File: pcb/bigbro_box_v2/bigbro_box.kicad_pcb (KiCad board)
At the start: 2 copper layers, 100 x 58 mm, 46 parts, among them J1 Current Sense, J2 Display, J3 Mains, J4 Debug, J5 RFID, J6 Relay, J7 Ext, K1 G5LE-1, Q1 MMBT3904, Q2 MMBT3904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

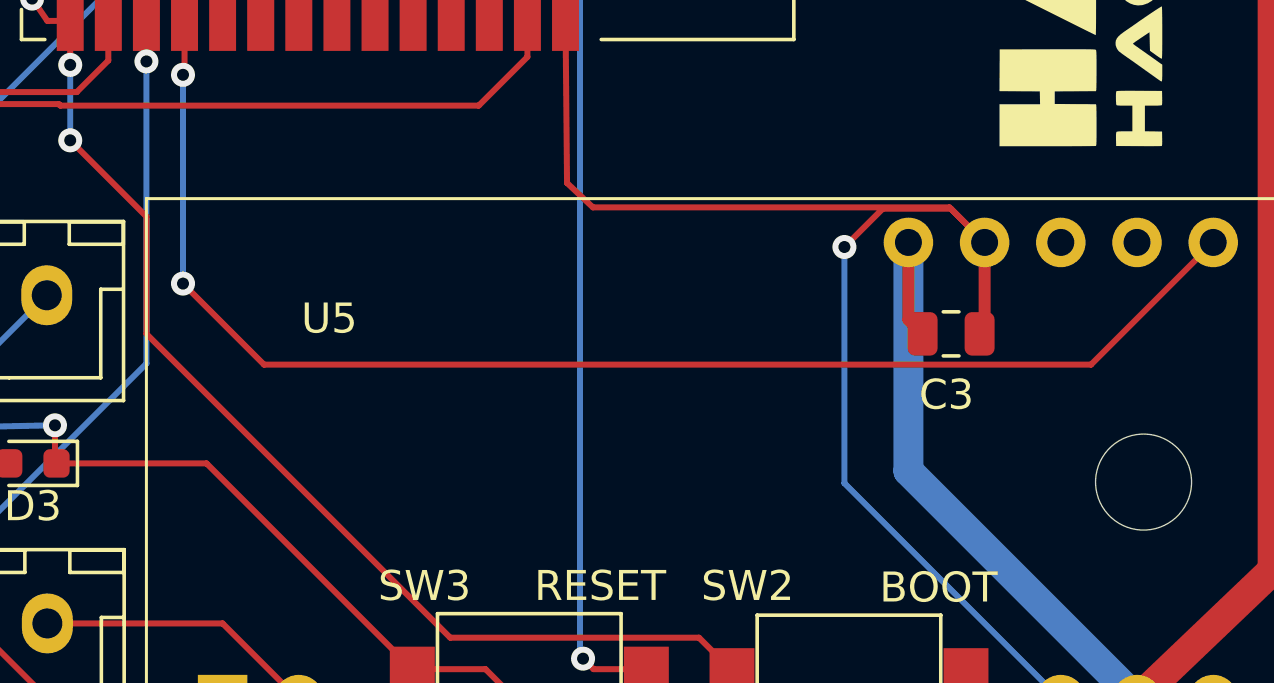
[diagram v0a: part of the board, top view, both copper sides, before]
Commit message: Add voltage divider for RFID.
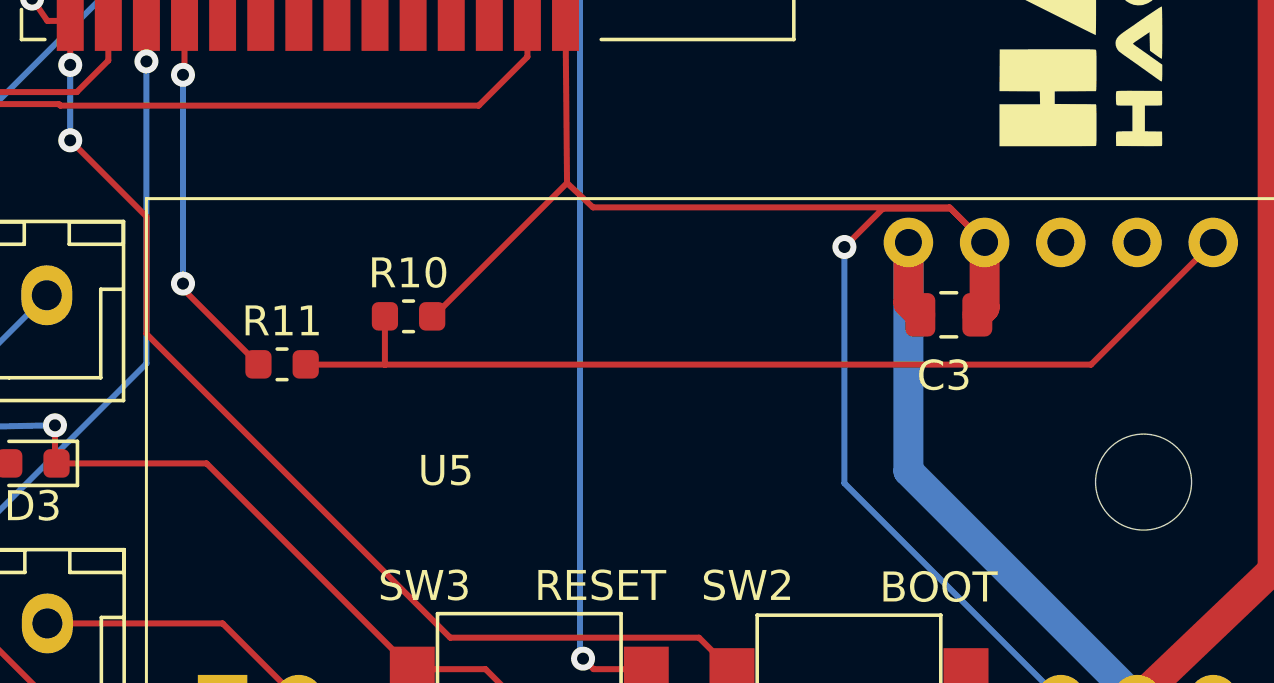
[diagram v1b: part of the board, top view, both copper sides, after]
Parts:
- added R10: 2k2, Resistor_SMD:R_0603_1608Metric, F.Cu at (136.5, 98.5)
- added R11: 1k2, Resistor_SMD:R_0603_1608Metric, F.Cu at (132.3, 100.1)
- moved C3 0.64 mm to (154.5, 98.4)
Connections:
- U5 pad 6: ESP_RFID_TX -> Net-(U5-TX)
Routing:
- net Net-(U5-TX): track 0.00 -> 33.6 mm
- net ESP_RFID_TX: track 45.9 -> 12.5 mm
- net GND: track 317.4 -> 323.1 mm
- net +5V: track 197.9 -> 197.3 mm

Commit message: Increase value of switch LED resistor.
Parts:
- R9: value 330 -> 680
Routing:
- net /~{BOOT}: track 67.5 -> 69.3 mm
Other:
- board text added: "https://github.com/hal9k-dk/bigbro"

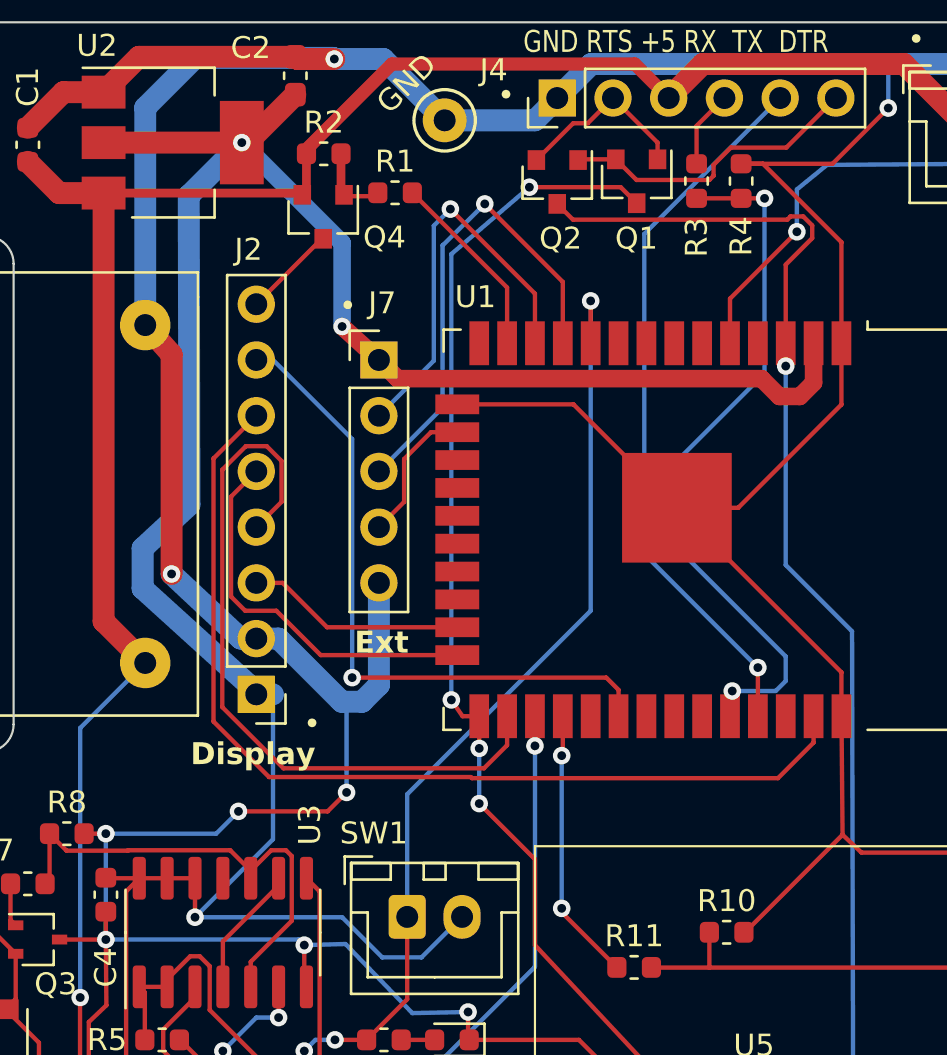
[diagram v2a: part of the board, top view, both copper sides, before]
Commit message: Flip display connector.
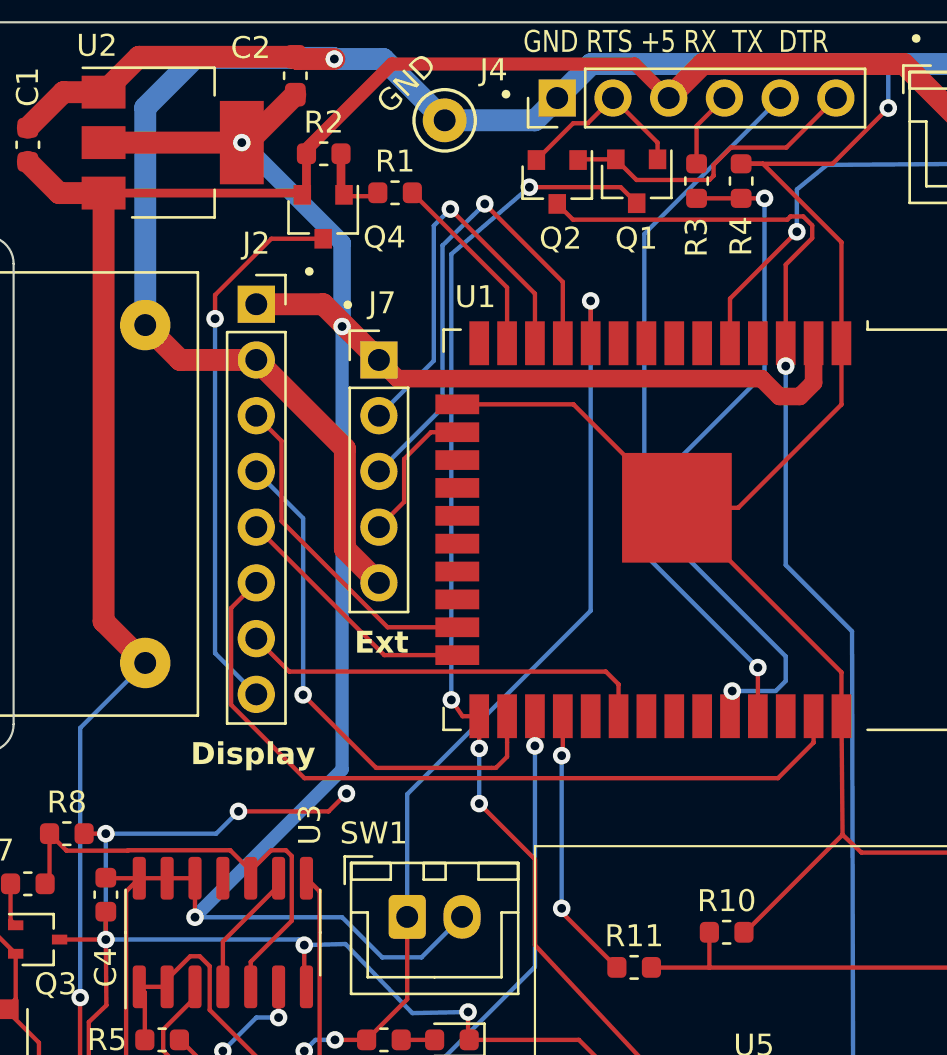
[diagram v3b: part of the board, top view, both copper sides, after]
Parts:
- J2: footprint Connector_PinHeader_2.54mm:PinHeader_1x08_P2.54mm_Vertical -> Connector_PinSocket_2.54mm:PinSocket_1x08_P2.54mm_Vertical
- moved J2 17.8 mm to (115.1, 69.9), turned to 0 degrees
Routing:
- net Display_Led: track 4.28 -> 25.0 mm, vias 0 -> 1
- net GND: track 323.1 -> 308.4 mm, vias 10 -> 9
- net Display_SCk: track 29.5 -> 18.8 mm, vias 1 -> 0
- net Display_Reset: track 33.6 -> 23.8 mm, vias 0 -> 1
- net Display_SDA: track 45.0 -> 35.8 mm
- net Display_A0: track 17.6 -> 11.6 mm
- net +3V3: track 117.7 -> 112.3 mm
- net Display_CS: track 10.00 -> 15.3 mm

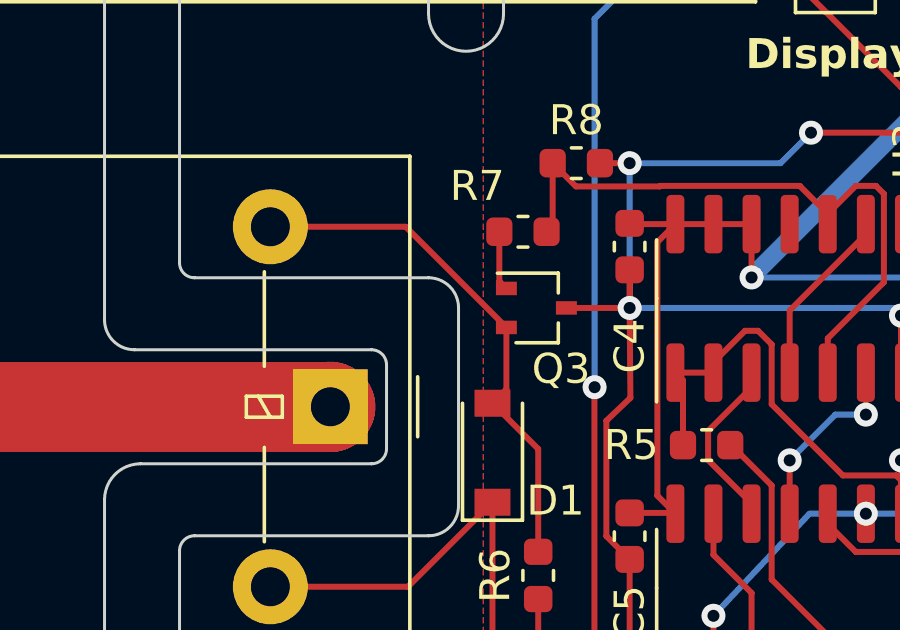
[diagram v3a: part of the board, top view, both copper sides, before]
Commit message: Swap S and D on Q3.
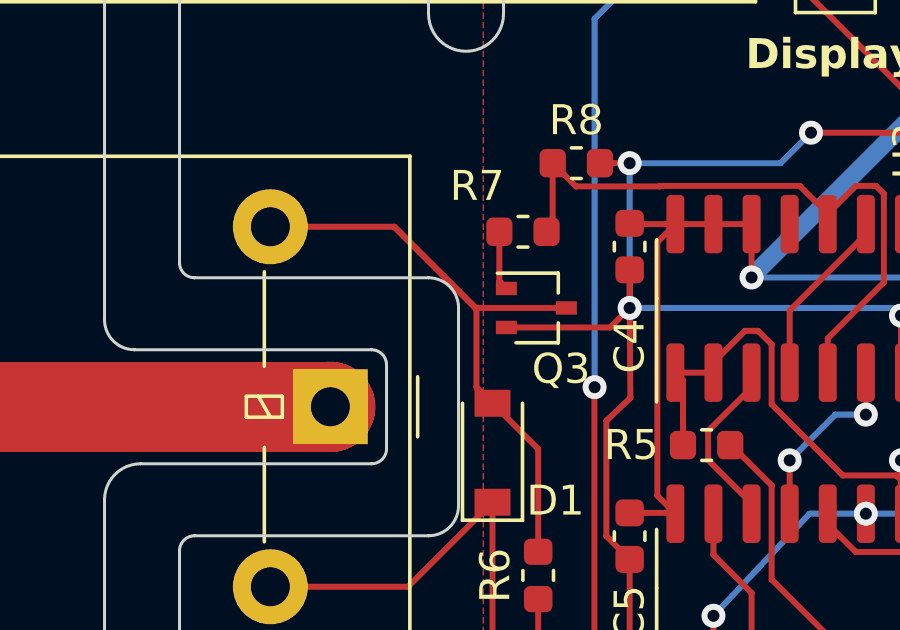
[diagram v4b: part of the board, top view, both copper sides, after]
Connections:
- Q3 pad 2: Net-(D1-A) -> GND
- Q3 pad 3: GND -> Net-(D1-A)
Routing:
- net Net-(D1-A): track 17.6 -> 23.8 mm
- net GND: track 308.4 -> 310.7 mm
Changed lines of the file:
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@@
     (property "Sheetfile" "bigbro_box.kicad_sch")
     (property "Sheetname" "")
-    (property "ki_description" "N-MOSFET transistor, gate/drain/source")
+    (property "ki_description" "N-MOSFET transistor, gate/source/drain")
     (property "ki_keywords" "transistor NMOS N-MOS N-MOSFET")
     (attr smd)
@@
       (net 21 "Net-(Q3-G)") (pinfunction "G") (pintype "input"))
     (pad "2" smd rect (at -1 0.65 270) (size 0.45 0.7) (layers "F.Cu" "F.Paste" "F.Mask")
+      (net 2 "GND") (pinfunction "S") (pintype "passive"))
+    (pad "3" smd rect (at 1 0 270) (size 0.45 0.7) (layers "F.Cu" "F.Paste" "F.Mask")
       (net 4 "Net-(D1-A)") (pinfunction "D") (pintype "passive"))
-    (pad "3" smd rect (at 1 0 270) (size 0.45 0.7) (layers "F.Cu" "F.Paste" "F.Mask")
-      (net 2 "GND") (pinfunction "S") (pintype "passive"))
     (model "${KICAD6_3DMODEL_DIR}/Package_TO_SOT_SMD.3dshapes/SOT-323_SC-70.wrl"
       (offset (xyz 0 0 0))
@@
   (segment (start 152.3058 94.887) (end 151.0284 96.1644) (width 0.2) (layer "F.Cu") (net 2))
   (segment (start 139.065 110.236) (end 140.6906 111.8616) (width 0.2) (layer "F.Cu") (net 2))
+  (segment (start 107.554 99.456) (end 108.204 98.806) (width 0.2) (layer "F.Cu") (net 2))
   (segment (start 118.618 58.674) (end 116.9405 58.674) (width 1) (layer "F.Cu") (net 2))
   (segment (start 141.3258 63.449) (end 143.8656 60.9092) (width 0.2) (layer "F.Cu") (net 2))
@@
   (segment (start 141.732 88.628) (end 141.7828 94.0308) (width 0.2) (layer "F.Cu") (net 2))
   (segment (start 153.506 111.8616) (end 155.0808 110.2868) (width 0.2) (layer "F.Cu") (net 2))
+  (segment (start 104.096 99.456) (end 107.554 99.456) (width 0.2) (layer "F.Cu") (net 2))
   (segment (start 109.391604 111.889) (end 114.171 111.889) (width 0.2) (layer "F.Cu") (net 2))
   (segment (start 155.702 96.012) (end 154.577 94.887) (width 0.2) (layer "F.Cu") (net 2))
   (segment (start 137.3378 98.4758) (end 141.7828 94.0308) (width 0.2) (layer "F.Cu") (net 2))
   (segment (start 114.808 111.252) (end 114.808 110.614) (width 0.2) (layer "F.Cu") (net 2))
-  (segment (start 108.204 98.806) (end 106.096 98.806) (width 0.2) (layer "F.Cu") (net 2))
   (segment (start 108.2294 101.8032) (end 108.204 98.806) (width 0.2) (layer "F.Cu") (net 2))
   (segment (start 115.061293 72.390707) (end 119.1005 76.429914) (width 1) (layer "F.Cu") (net 2))
@@
   (segment (start 122.5942 99.6188) (end 124.44 97.773) (width 0.2) (layer "B.Cu") (net 3))
   (segment (start 118.9736 97.79) (end 120.8024 99.6188) (width 0.2) (layer "B.Cu") (net 3))
-  (segment (start 104.096 101.518) (end 103.632 101.982) (width 0.2) (layer "F.Cu") (net 4))
+  (segment (start 103.0976 98.838299) (end 103.0976 101.4476) (width 0.2) (layer "F.Cu") (net 4))
+  (segment (start 100.359301 96.1) (end 96.2275 96.1) (width 0.2) (layer "F.Cu") (net 4))
+  (segment (start 103.0976 101.4476) (end 103.632 101.982) (width 0.2) (layer "F.Cu") (net 4))
+  (segment (start 103.065301 98.806) (end 100.359301 96.1) (width 0.2) (layer "F.Cu") (net 4))
   (segment (start 105.156 103.506) (end 103.632 101.982) (width 0.2) (layer "F.Cu") (net 4))
   (segment (start 105.156 106.934) (end 105.156 103.506) (width 0.2) (layer "F.Cu") (net 4))
-  (segment (start 104.096 99.456) (end 104.096 101.518) (width 0.2) (layer "F.Cu") (net 4))
-  (segment (start 104.096 99.456) (end 100.74 96.1) (width 0.2) (layer "F.Cu") (net 4))
-  (segment (start 100.74 96.1) (end 96.2275 96.1) (width 0.2) (layer "F.Cu") (net 4))
+  (segment (start 106.096 98.806) (end 103.065301 98.806) (width 0.2) (layer "F.Cu") (net 4))
+  (segment (start 100.359301 96.1) (end 103.0976 98.838299) (width 0.2) (layer "F.Cu") (net 4))
   (segment (start 105.156 110.693) (end 105.207 110.744) (width 0.2) (layer "F.Cu") (net 5))
   (segment (start 105.156 108.509) (end 105.156 110.693) (width 0.2) (layer "F.Cu") (net 5))
